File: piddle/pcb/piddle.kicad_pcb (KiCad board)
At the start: 2 copper layers, 133.5 x 118 mm, 65 parts, among them J1 Conn_01x03_Socket, J10 Conn_01x03_Socket, J11 Conn_01x02_Socket, J12 Conn_01x02_Socket, J13 Conn_01x02_Pin, J2 Conn_01x03_Socket, J3 Conn_01x03_Socket, J4 Conn_01x03_Socket, J5 Conn_01x03_Socket, J6 Conn_01x03_Socket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

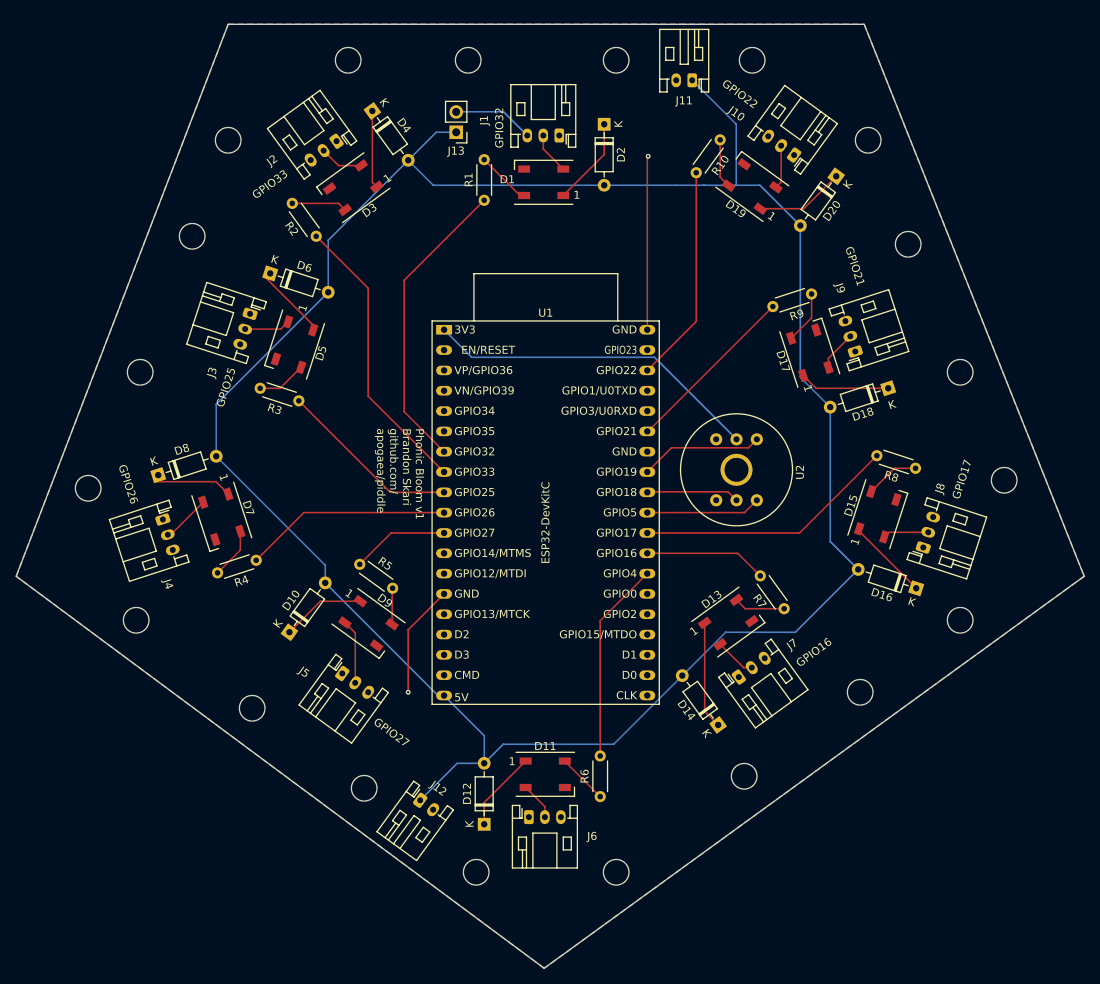
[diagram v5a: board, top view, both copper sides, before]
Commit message: Use SMD resistors
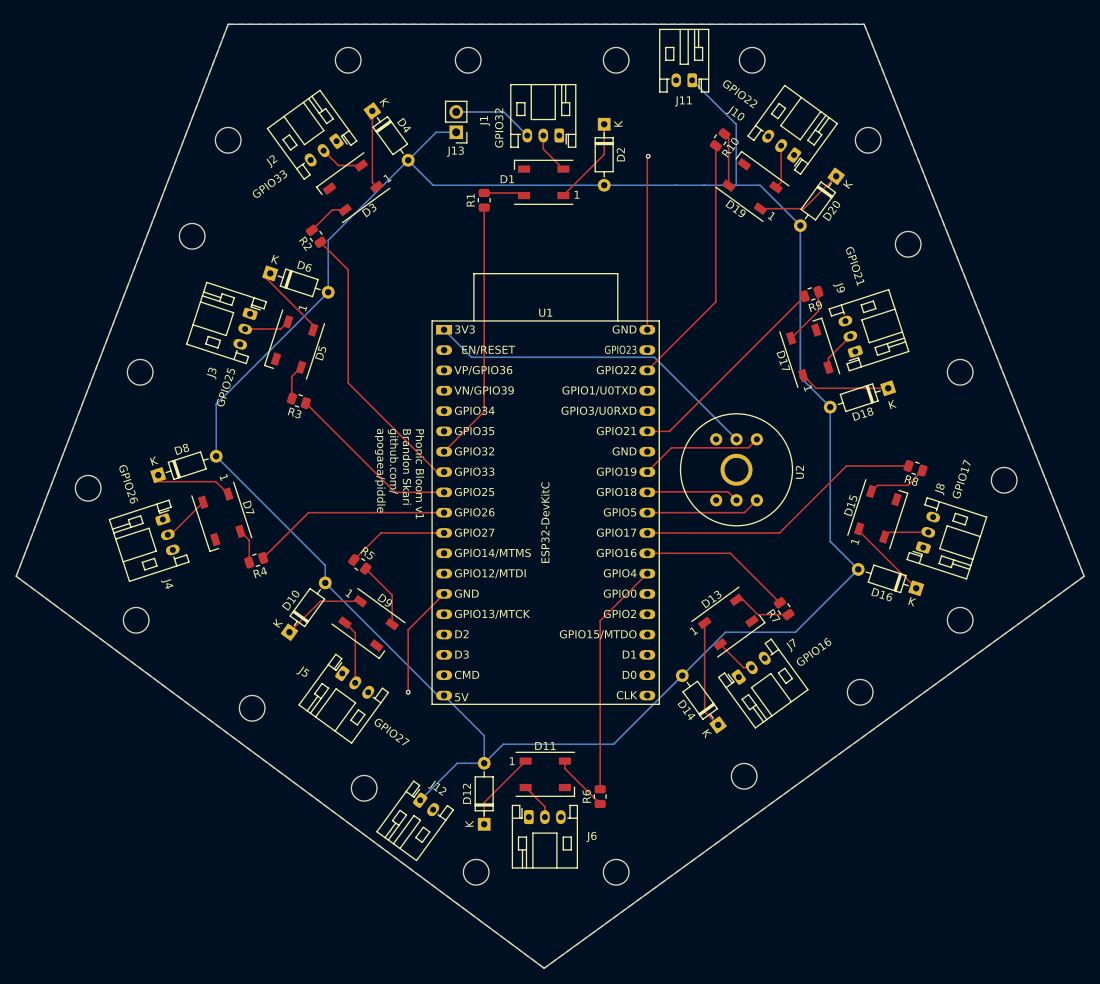
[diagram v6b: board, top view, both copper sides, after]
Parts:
- R1, R10, R2, R3, R4, R5, R6, R7, R8, R9: value R -> 200; footprint Resistor_THT:R_Axial_DIN0204_L3.6mm_D1.6mm_P5.08mm_Horizontal -> Resistor_SMD:R_0805_2012Metric
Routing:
- net /GPIO32: track 37.6 -> 32.6 mm
- net /GPIO21: track 22.2 -> 26.7 mm
- net /GPIO22: track 27.2 -> 31.6 mm
- net /GPIO4: track 25.2 -> 29.4 mm
- net /GPIO16: track 15.3 -> 19.1 mm
- net Net-(D9-DIN): track 4.53 -> 8.33 mm
- net /GPIO17: track 32.7 -> 36.1 mm
- net Net-(D7-DIN): track 6.37 -> 4.36 mm
- net Net-(D5-DIN): track 6.20 -> 4.39 mm
- net Net-(D3-DIN): track 6.94 -> 5.21 mm
- net Net-(D1-DIN): track 6.84 -> 5.62 mm
- net /GPIO26: track 26.0 -> 25.0 mm
- net /GPIO25: track 22.9 -> 21.9 mm
- net Net-(D11-DIN): track 6.26 -> 7.18 mm
- net Net-(D13-DIN): track 6.43 -> 7.27 mm
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
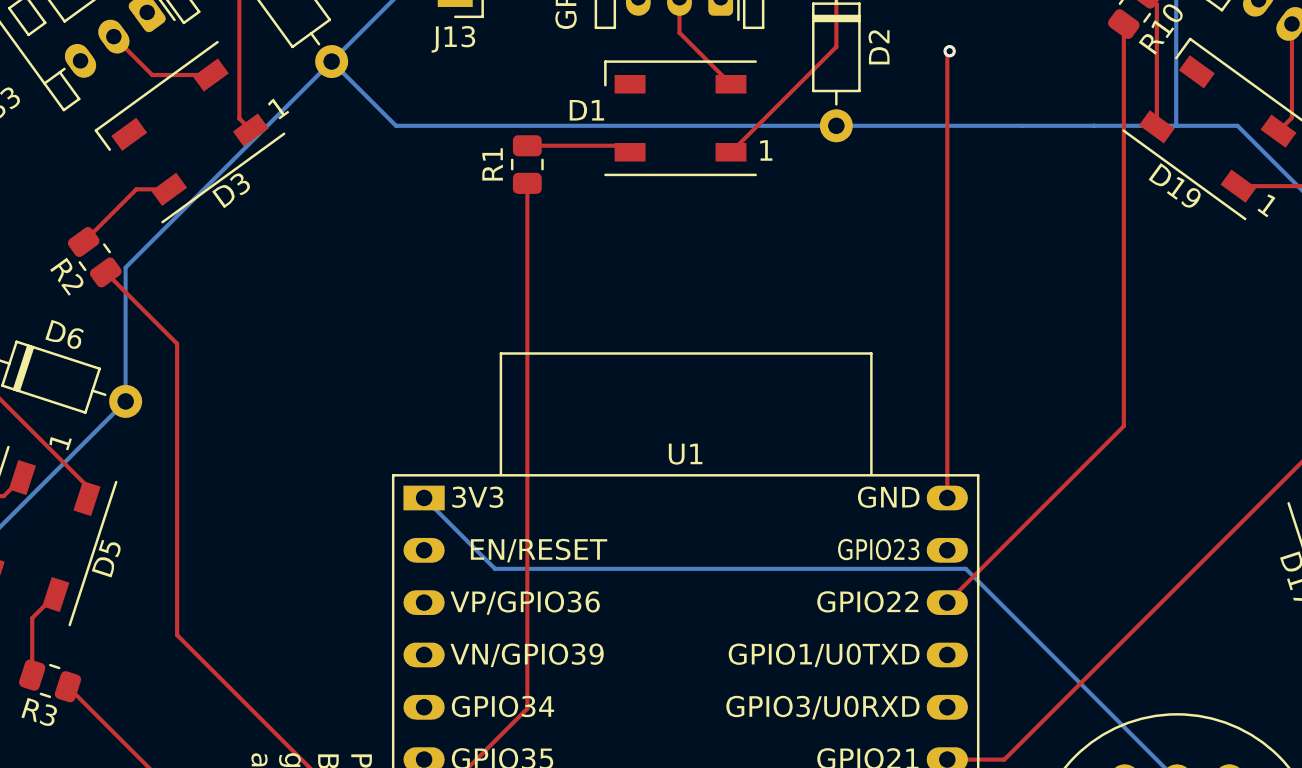
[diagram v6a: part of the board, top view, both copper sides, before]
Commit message: Add voltage divider
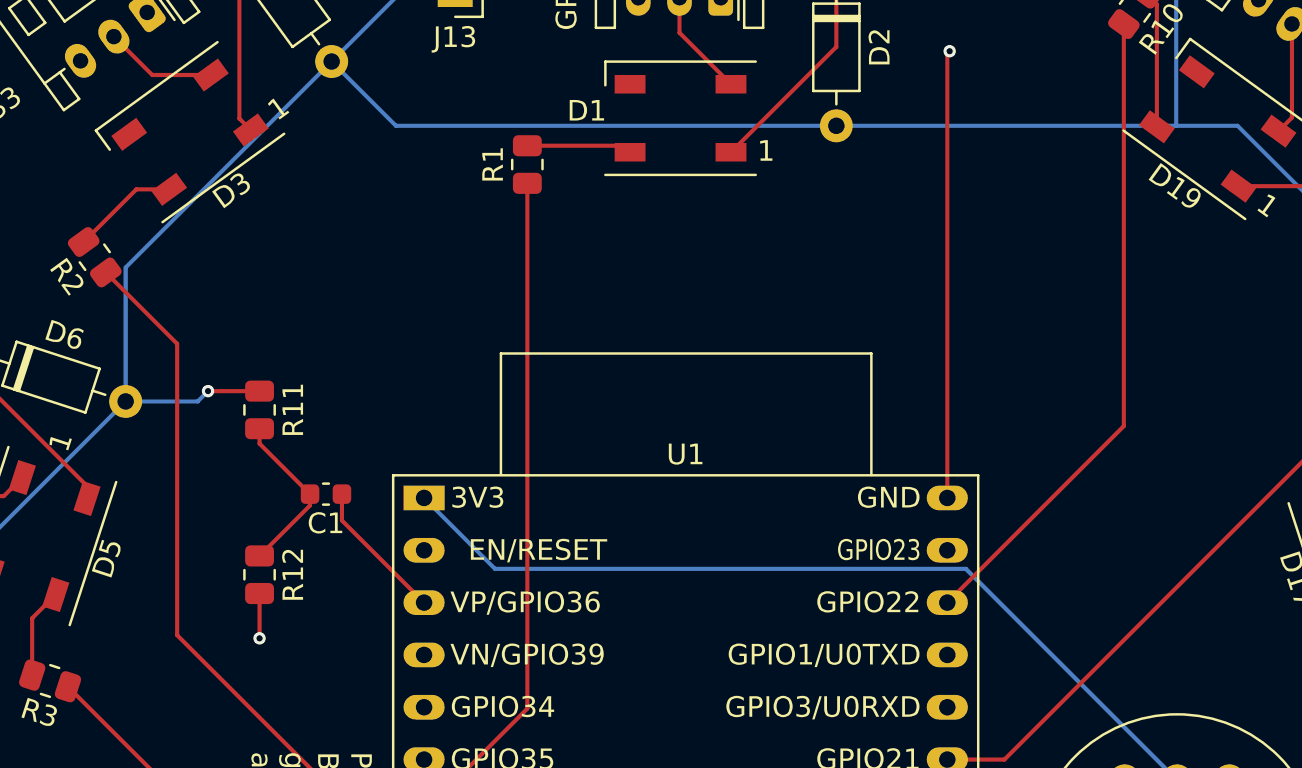
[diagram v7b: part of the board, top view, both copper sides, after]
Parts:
- added C1: 0.1uF, Capacitor_SMD:C_0603_1608Metric, F.Cu at (87.8, 92.1)
- added R11: 10000, Resistor_SMD:R_0805_2012Metric, F.Cu at (84.6, 88.0)
- added R12: 10000, Resistor_SMD:R_0805_2012Metric, F.Cu at (84.6, 96.0)
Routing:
- net Net-(C1-Pad2): track 0.00 -> 8.20 mm
- net +5V: track 287.6 -> 294.8 mm, vias 0 -> 1
- net /GPIO36: track 0.00 -> 6.92 mm
- net GND: track 35.9 -> 38.1 mm, vias 2 -> 3

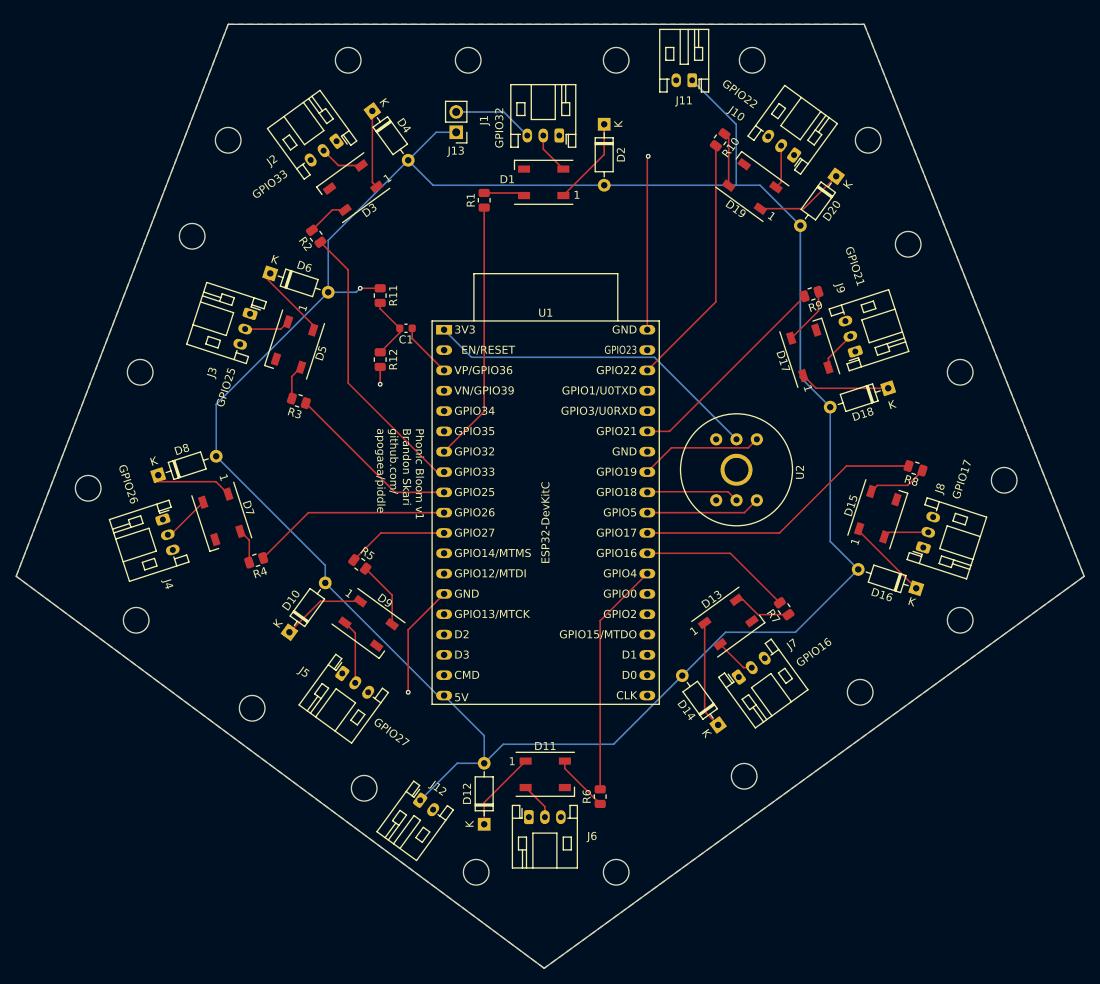
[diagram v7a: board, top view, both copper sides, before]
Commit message: FLip the connectors
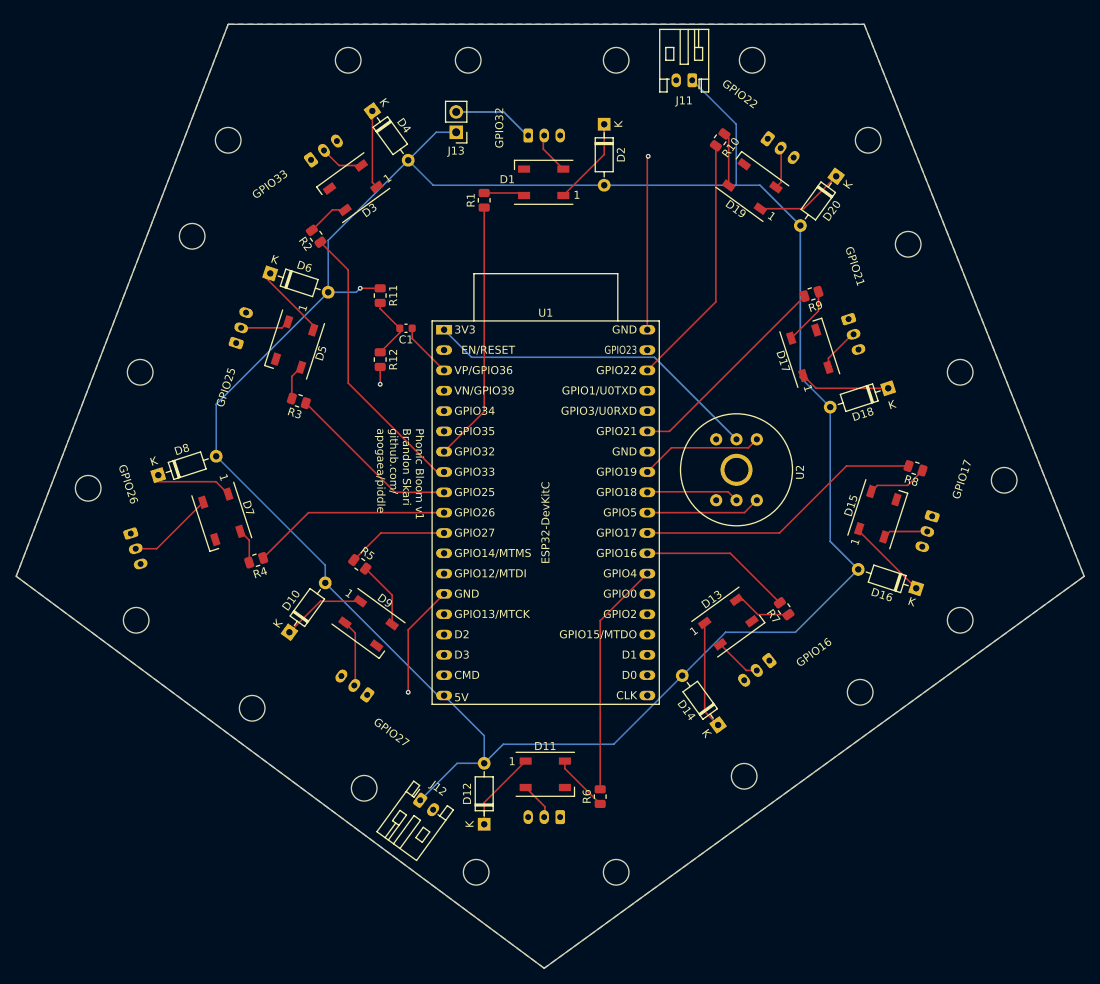
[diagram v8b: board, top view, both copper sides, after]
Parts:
- J1, J10, J2, J3, J4, J5, J6, J7, J8, J9: moved to B.Cu
- moved J4 4.38 mm to (53.4, 117.8)
- moved J7 4.34 mm to (133.3, 133.6), turned to -142 degrees
- moved J9 4.13 mm to (143.2, 91.0), turned to -72 degrees
- moved J5 4.11 mm to (83.0, 137.9), turned to 144 degrees
- moved J8 4.06 mm to (153.6, 115.6), turned to -108 degrees
- moved J3 4.04 mm to (66.6, 93.9), turned to 72 degrees
- moved J2 3.95 mm to (76.0, 71.0), turned to 36 degrees
- moved J6 3.91 mm to (107.1, 153.2), turned to 180 degrees
- moved J1 3.89 mm to (103.1, 68.0), turned to 0 degrees
- moved J10 3.88 mm to (133.1, 68.4), turned to -36 degrees
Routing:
- net Net-(D7-DOUT): track 6.10 -> 10.8 mm
- net Net-(D13-DOUT): track 5.16 -> 5.93 mm
